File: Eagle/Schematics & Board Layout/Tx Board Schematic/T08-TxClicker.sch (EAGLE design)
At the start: 86 parts, among them U1 CC430F513X---RGZ48, Y1 26MHz

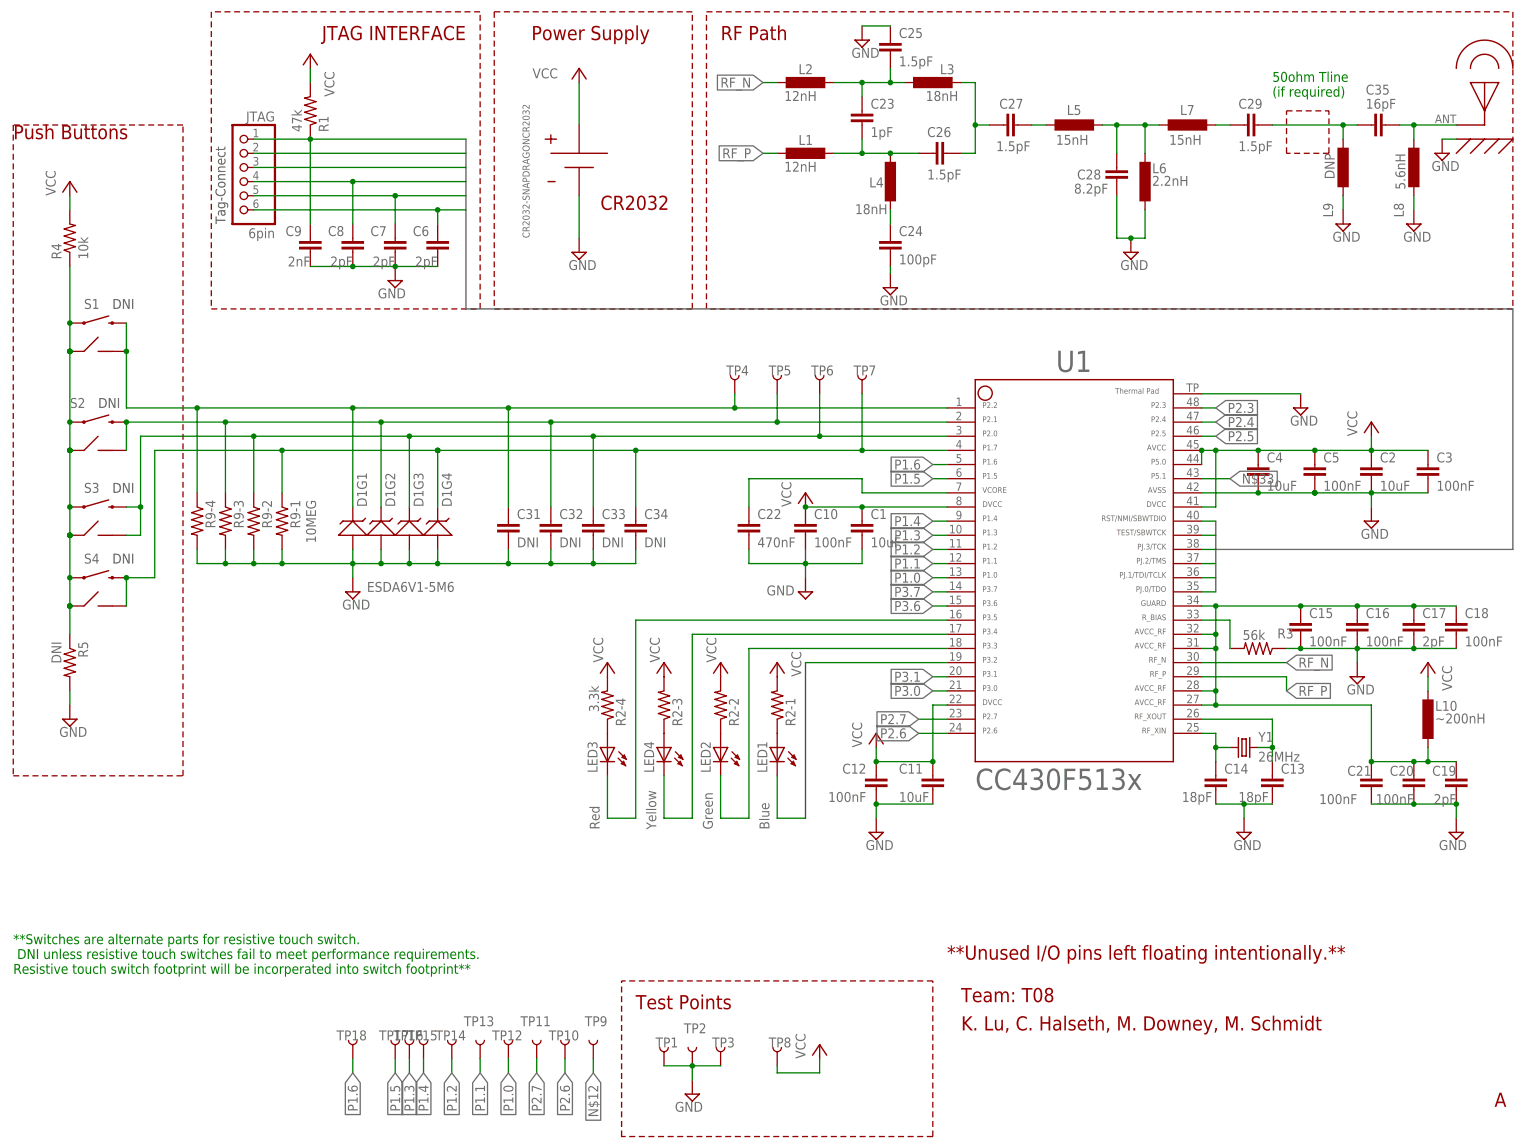
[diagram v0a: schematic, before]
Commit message: Eagle BRD Layout
Incomplete, first pass layout
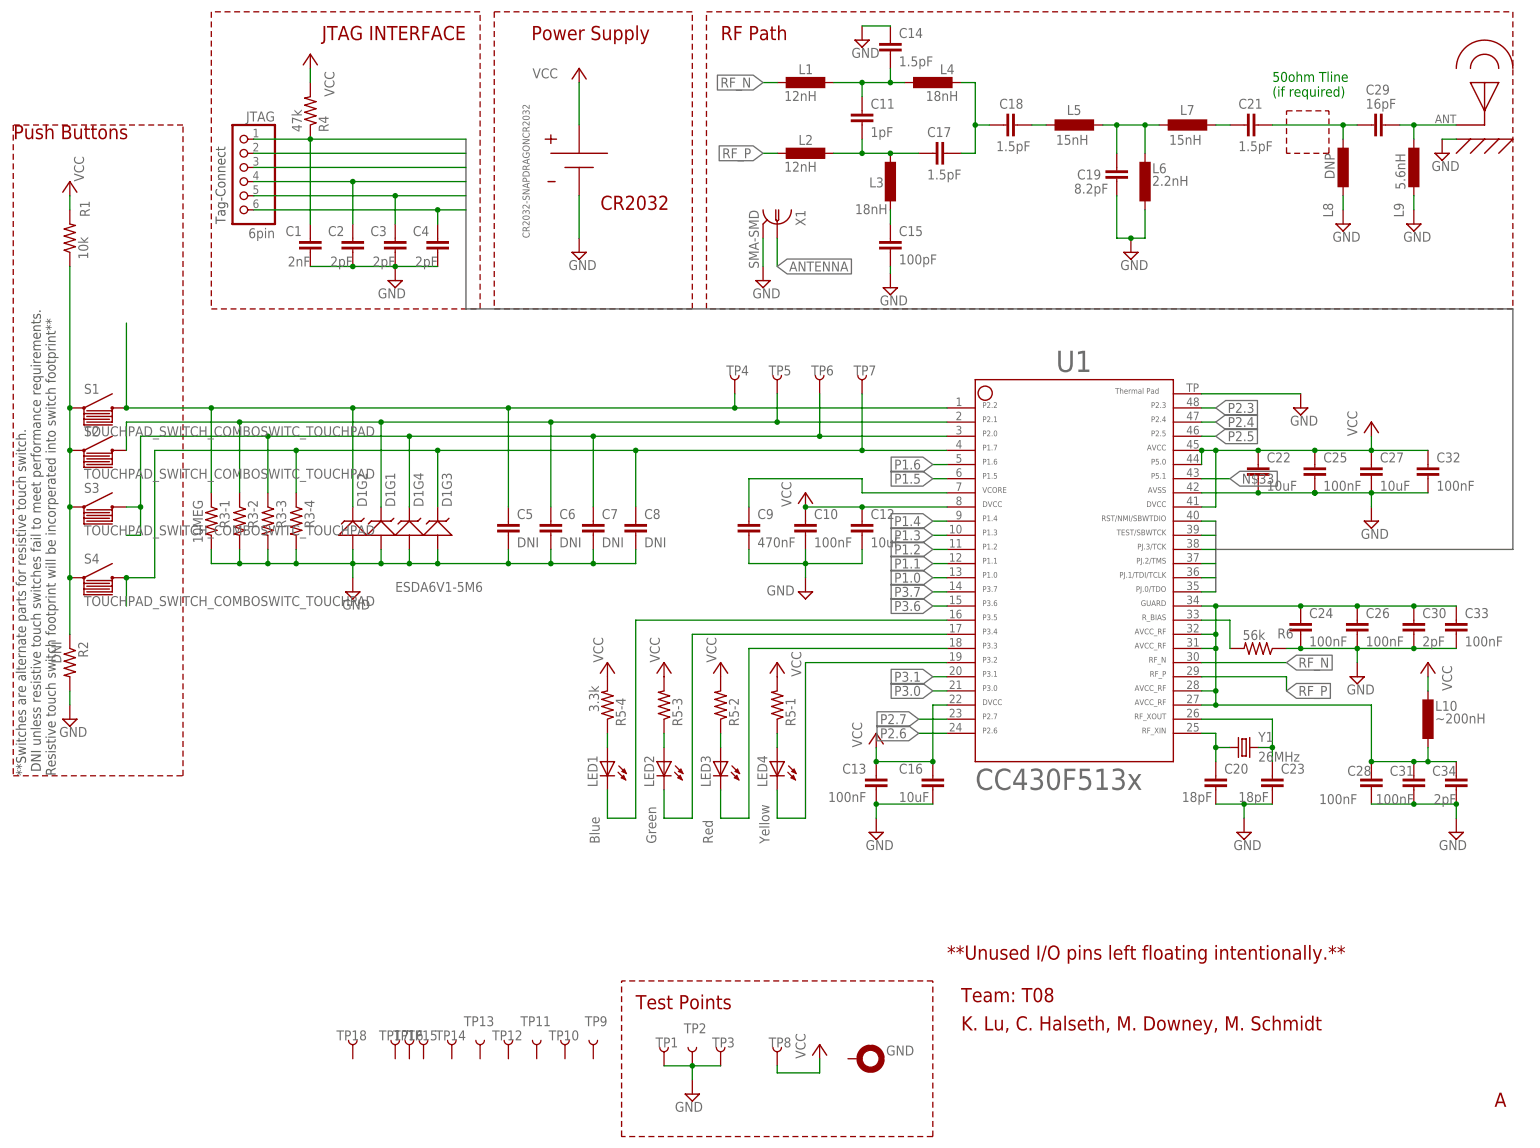
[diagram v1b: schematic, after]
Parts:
- removed C35: 16pF, rcl:C-EUC0402
- removed R9: 10MEG, QuadResistor:R603X42012
- removed U$1, U$3, U$4: TOUCH-PAD, TouchPad:TOUCH-PAD
- removed U$2: CR2032-SNAPDRAGONCR2032, CR2032-SnapDragon:CR2032-SNAPDRAGONCR2032
- added C30: 2pF, rcl:C-EUC0603
- added GND: (no value), SparkFun-Connectors:STARBOARD_GND-SMALL2
- added R6: 56k, rcl:R-US_R0603
- added X1: SMA-SMD, con-coax:SMA-SMD
- C1: value 10uF -> 2nF; device rcl:C-EUC0805 -> rcl-amber:C0603
- C11: value 10uF -> 1pF; device rcl:C-EUC0805 -> rcl:C-EUC0402
- C12, C16: value 100nF -> 10uF; device rcl:C-EUC0603 -> rcl:C-EUC0805
- C13: value 18pF -> 100nF; device rcl:C-EUC0402 -> rcl:C-EUC0603
- C14: value 18pF -> 1.5pF
- C15: value 100nF -> 100pF; device rcl:C-EUC0603 -> rcl:C-EUC0402
- C17: value 2pF -> 1.5pF; device rcl:C-EUC0603 -> rcl:C-EUC0402
- C18, C21: value 100nF -> 1.5pF; device rcl:C-EUC0603 -> rcl:C-EUC0402
- C19: value 2pF -> 8.2pF; device rcl:C-EUC0603 -> rcl:C-EUC0402
- C2, C4: value 10uF -> 2pF; device rcl:C-EUC0805 -> rcl-amber:C0603
- C20: value 100nF -> 18pF; device rcl:C-EUC0603 -> rcl:C-EUC0402
- C22: value 470nF -> 10uF; device rcl:C-EUC0603 -> rcl:C-EUC0805
- C23: value 1pF -> 18pF
- C24: value 100pF -> 100nF; device rcl:C-EUC0402 -> rcl:C-EUC0603
- C25, C26: value 1.5pF -> 100nF; device rcl:C-EUC0402 -> rcl:C-EUC0603
- C27: value 1.5pF -> 10uF; device rcl:C-EUC0402 -> rcl:C-EUC0805
- C28: value 8.2pF -> 100nF; device rcl:C-EUC0402 -> rcl:C-EUC0603
- C29: value 1.5pF -> 16pF
- C3: value 100nF -> 2pF; device rcl:C-EUC0603 -> rcl-amber:C0603
- C31, C32, C33: value DNI -> 100nF
- C34: value DNI -> 2pF
- C5: value 100nF -> DNI
- C6, C7, C8: value 2pF -> DNI; device rcl-amber:C0603 -> rcl:C-EUC0603
- C9: value 2nF -> 470nF; device rcl-amber:C0603 -> rcl:C-EUC0603
- L8: value 5.6nH -> DNP
- L9: value DNP -> 5.6nH
- R1: value 47k -> 10k
- R2: value 3.3k -> DNI; device QuadResistor:R603X42012 -> rcl:R-US_R0603
- R3: value 56k -> 10MEG; device rcl:R-US_R0603 -> QuadResistor:R603X42012
- R4: value 10k -> 47k
- R5: value DNI -> 3.3k; device rcl:R-US_R0603 -> QuadResistor:R603X42012
- S1, S2, S3, S4: value SWITCH-MOMENTARY-212MM -> TOUCHPAD_SWITCH_COMBOSWITC_TOUCHPAD; device SparkFun-Electromechanical:SWITCH-MOMENTARY-212MM -> SparkFun-Electromechanical--edited:TOUCHPAD_SWITCH_COMBOSWITC_TOUCHPAD
- U$5: value TOUCH-PAD -> CR2032-SNAPDRAGONCR2032; device TouchPad:TOUCH-PAD -> CR2032-SnapDragon:CR2032-SNAPDRAGONCR2032
- renumbered U$7 to U$6
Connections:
- removed net N$10: C35.1, L8.2, U$6.ANT
- removed net N$12: TP9.1
- removed net N$18: LED1.A, R2-1.1
- removed net N$21: LED3.A, R2-4.1
- removed net N$23: LED4.A, R2-3.1
- removed net N$24: LED2.A, R2-2.1
- new net ANTENNA: C29.1, L9.2, U$6.ANT, X1.1
- new net N$13: LED1.A, R5-4.1
- new net N$14: LED2.A, R5-3.1
- new net N$16: LED3.A, R5-2.1
- new net N$17: LED4.A, R5-1.1
- net GND: now also C14.1, C19.1, C23.2, C25.2, C26.2, C27.2, C28.2, C30.2, R2.2, R3-1.2, R3-2.2, R3-3.2, R3-4.2, R6.1, U$5.V-, X1.2; no longer C11.2, C14.2, C17.2, C18.2, C19.2, C21.2, C25.1, C28.1, R3.1, R5.2, R9-1.2, R9-2.2, R9-3.2, R9-4.2, U$2.V-
- net N$1: now also C11.2, C17.2, L2.1, L3.1; no longer C23.2, C26.2, L1.1, L4.1
- net N$2: now also C11.1, C14.2, L1.1, L4.2; no longer C23.1, C25.2, L2.1, L3.2
- net N$20: now also R1.1, R2.1; no longer R4.1, R5.1, U$1.P$1, U$1.P$3, U$1.P$4, U$1.P$5, U$3.P$1, U$3.P$3, U$3.P$4, U$3.P$5, U$4.P$1, U$4.P$3, U$4.P$4, U$4.P$5, U$5.P$1, U$5.P$3, U$5.P$4, U$5.P$5
- net N$3: now also C17.1, C18.1, L4.1; no longer C26.1, C27.1, L3.1
- net N$4: now also C15.1, L3.2; no longer C24.1, L4.2
- net N$5: now also C18.2; no longer C27.2
- net N$6: now also C19.2; no longer C28.2
- net N$7: now also C21.1, C29.2, L8.2; no longer C29.1, C35.2, L9.2
- net N$8: now also C21.2; no longer C29.2
- net N$9: now also C24.1, C26.1, C28.1, C30.1, C31.1, C33.1, C34.1; no longer C15.1, C16.1, C17.1, C18.1, C19.1, C20.1, C21.1
- net P1.0: no longer TP12.1
- net P1.1: no longer TP13.1
- net P1.2: no longer TP14.1
- net P1.3: no longer TP16.1
- net P1.4: no longer TP15.1
- net P1.5: no longer TP17.1
- net P1.6: no longer TP18.1
- net P1.7: now also C8.1, D1G3.P$1, R3-4.1; no longer C34.1, D1G4.P$1, R9-1.1, U$1.VCC
- net P2.0: now also C7.1, D1G4.P$1, R3-3.1; no longer C33.1, D1G3.P$1, R9-2.1, U$3.VCC
- net P2.1: now also C6.1, D1G1.1, R3-2.1; no longer C32.1, D1G2.P$1, R9-3.1, U$4.VCC
- net P2.2: now also C5.1, D1G2.P$1, R3-1.1; no longer C31.1, D1G1.1, R9-4.1, U$5.VCC
- net P2.6: no longer TP10.1
- net P2.7: no longer TP11.1
- net P3.2: now also LED4.C; no longer LED1.C
- net P3.3: now also LED3.C; no longer LED2.C
- net P3.4: now also LED2.C; no longer LED4.C
- net P3.5: now also LED1.C; no longer LED3.C
- net PJ.0/TDO: now also C4.1; no longer C6.1
- net PJ.1/TDI/TCLK: now also C3.1; no longer C7.1
- net PJ.2/TMS: now also C2.1; no longer C8.1
- net RF_N: now also L1.2; no longer L2.2
- net RF_P: now also L2.2; no longer L1.2
- net RF_XIN: now also C20.1; no longer C14.1
- net RF_XOUT: now also C23.1; no longer C13.1
- net RST/NMI/SBWTDIO: now also C1.1, R4.1; no longer C9.1, R1.1
- net R_BIAS: now also R6.2; no longer R3.2
- net VCC: now also C13.1, C16.1, C22.1, C25.1, C27.1, C32.1, R5-1.2, R5-2.2, R5-3.2, R5-4.2, U$5.V+; no longer C1.1, C11.1, C2.1, C3.1, C4.1, C5.1, R2-1.2, R2-2.2, R2-3.2, R2-4.2, U$2.V+
- net VCORE: now also C9.1; no longer C22.1
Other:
- note removed: "DNI"
- moved on the sheet: C1, C11, C12, C13, C14, C15, C16, C17, C18, C19, C2, C20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

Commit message: Layout works
o.O
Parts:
- removed X1: SMA-SMD, con-coax:SMA-SMD
- added R7: 0-DNI, rcl-amber:R0603
- added X1-DNI: SMA-SMD, con-coax:SMA-SMD
- C11, C14, C15, C17, C18, C19, C21, C29: device rcl:C-EUC0402 -> rcl-amber:C0402
- L1, L2, L3, L4, L5, L6, L7, L8, L9: device rcl-amber:LL0603 -> rcl-amber:LL0402
- L10: device rcl-amber:LL0402 -> rcl-amber:LL0603
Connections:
- net N$33 renamed P5.1
- removed net N$7: C21.1, C29.2, L8.2
- new net N$10: R7.2, X1-DNI.1
- new net N$12: C21.1, C29.2, L8.2, R7.1
- net ANTENNA: no longer X1.1
- net GND: now also X1-DNI.2; no longer X1.2
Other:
- moved on the sheet: R1, R2

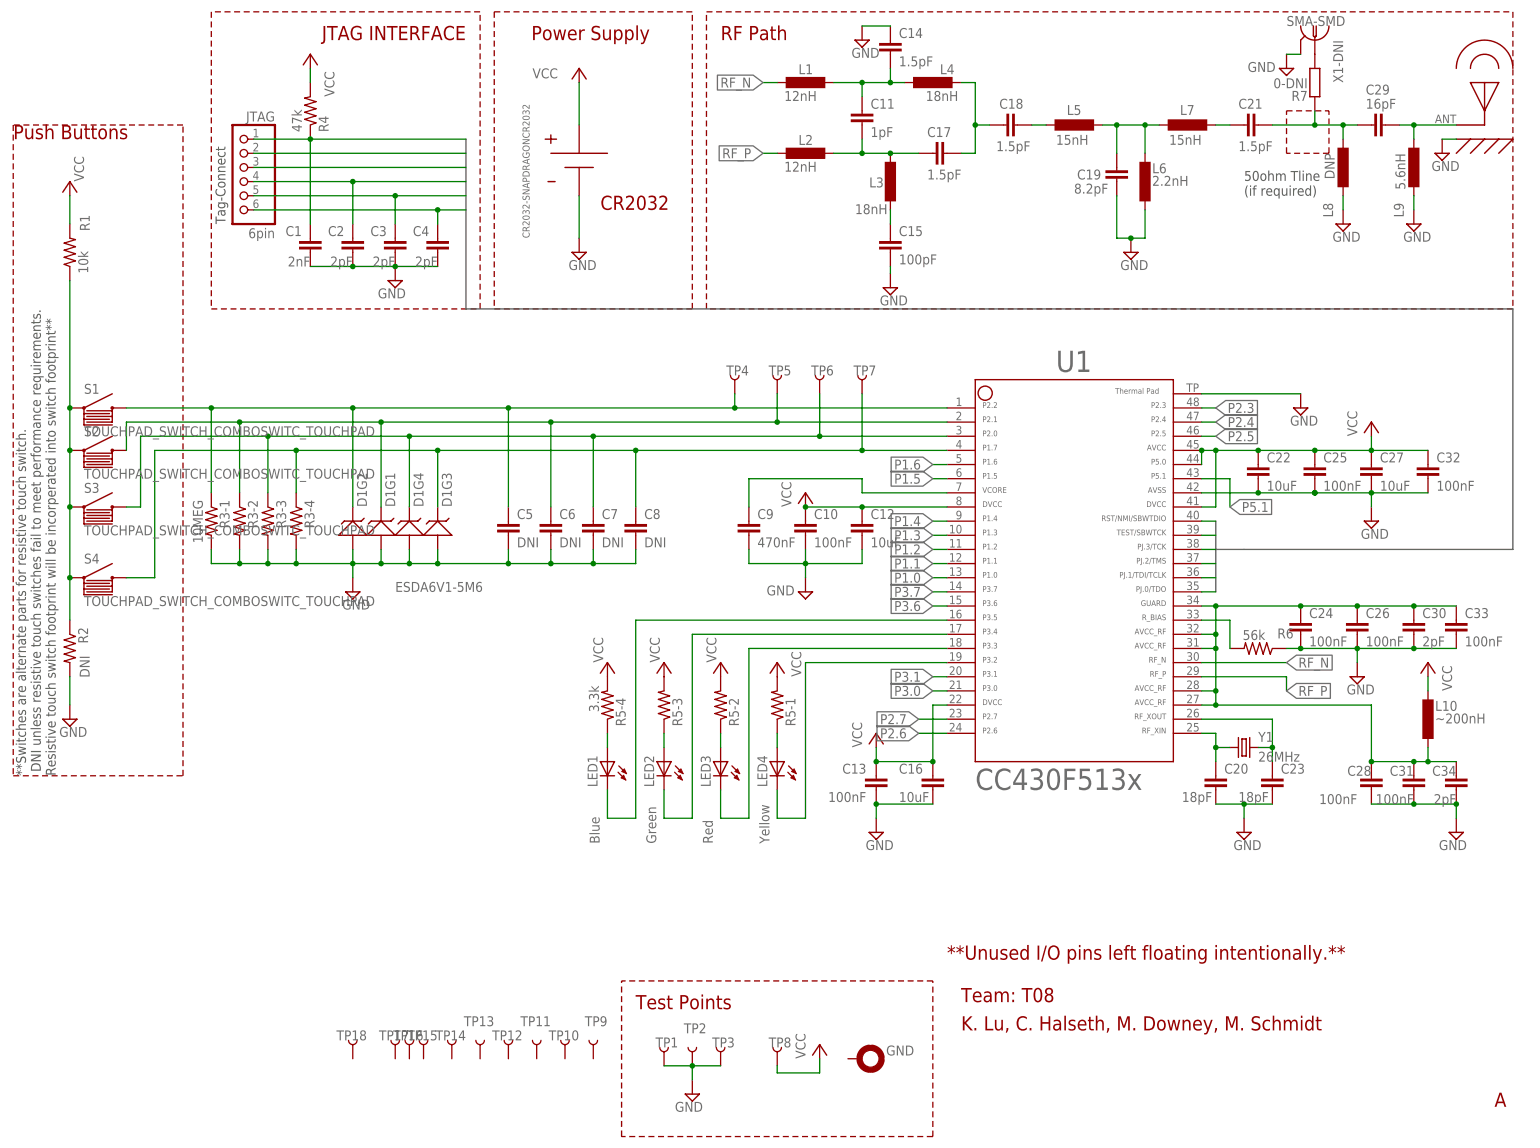
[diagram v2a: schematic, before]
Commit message: Eagle BRD Layout (rough)
Squawk list:
1) Antenna Pad
2) Pushbutton pad
3) VCC
4) Capacitors not near pins
5) Must optimize routing
6) Add ground test point
7) Fix GPIO Test points in schematic
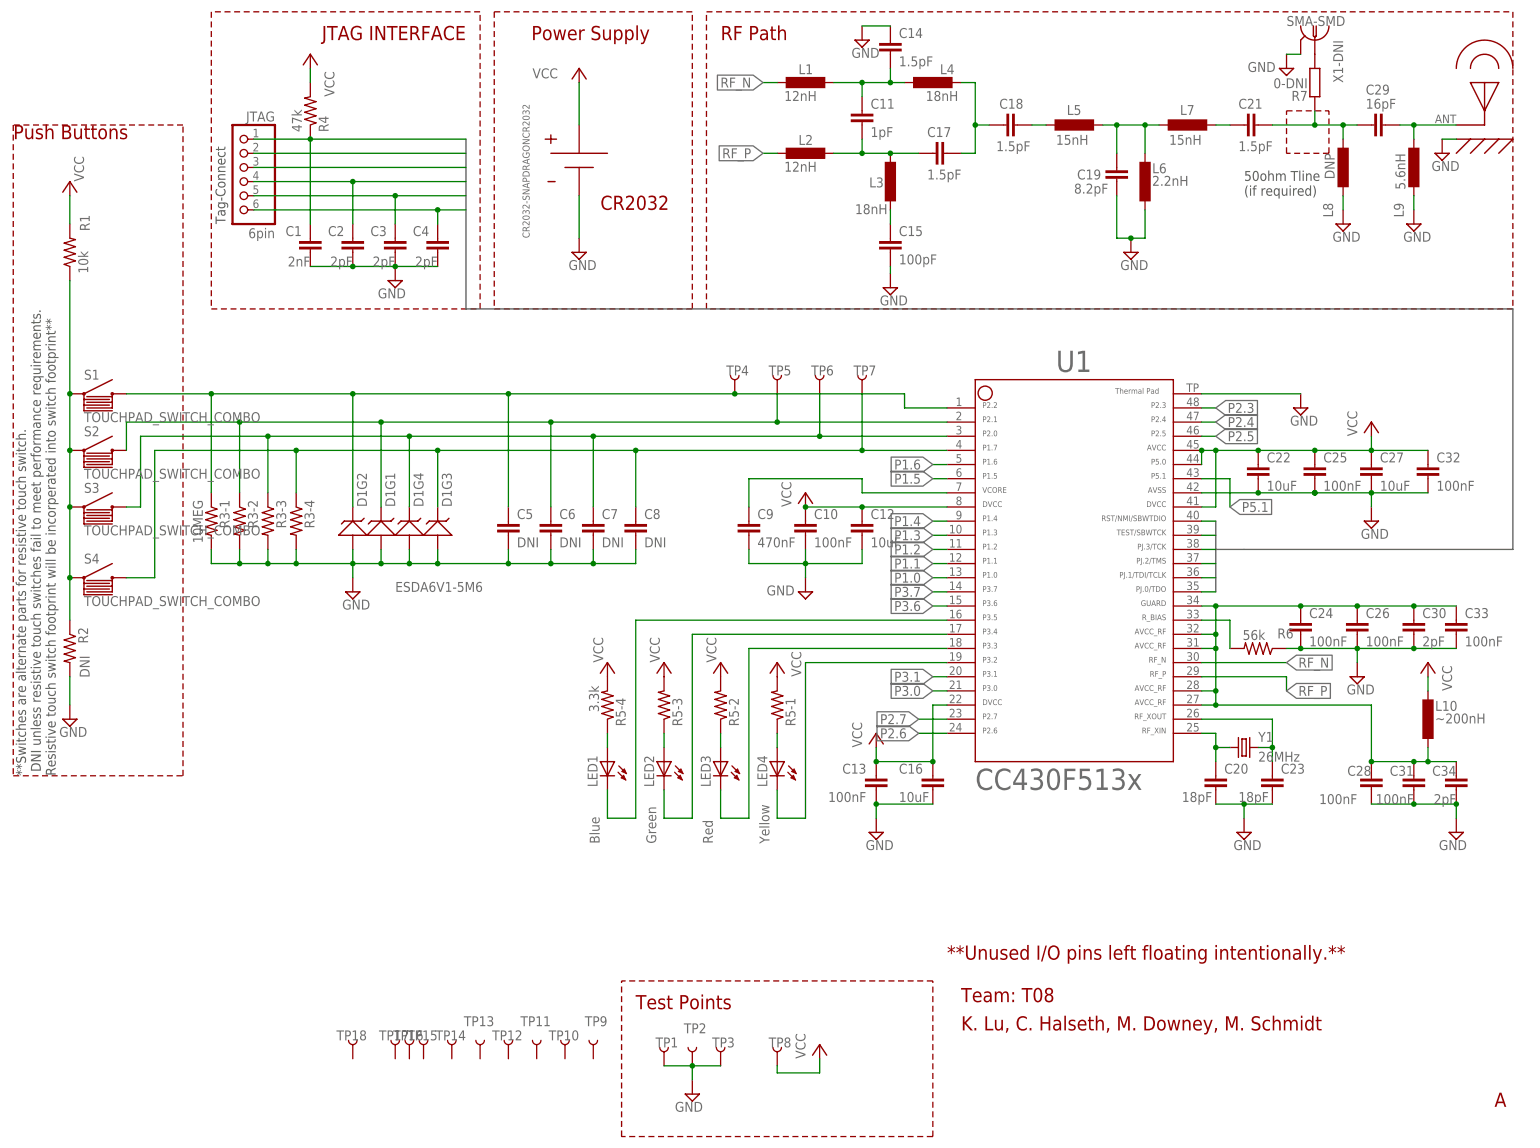
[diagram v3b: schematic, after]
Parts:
- removed GND: (no value), SparkFun-Connectors:STARBOARD_GND-SMALL2
- S1, S2, S3, S4: value TOUCHPAD_SWITCH_COMBOSWITC_TOUCHPAD -> TOUCHPAD_SWITCH_COMBO; device SparkFun-Electromechanical--edited:TOUCHPAD_SWITCH_COMBOSWITC_TOUCHPAD -> SparkFun-Electromechanical--edited:TOUCHPAD_SWITCH_COMBO
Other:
- moved on the sheet: S1
